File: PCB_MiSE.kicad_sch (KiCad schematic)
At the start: 35 parts, among them IC1 MSP430FR2355TPT, J1 WIFI, J2 Conn_01x03, J4 Clk read conn, J6 Display, J7 I2C read, J8 Conn_02x07_Odd_Even, SW1 SW_Push, SW2 SW_Push, SW3 SW_Push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

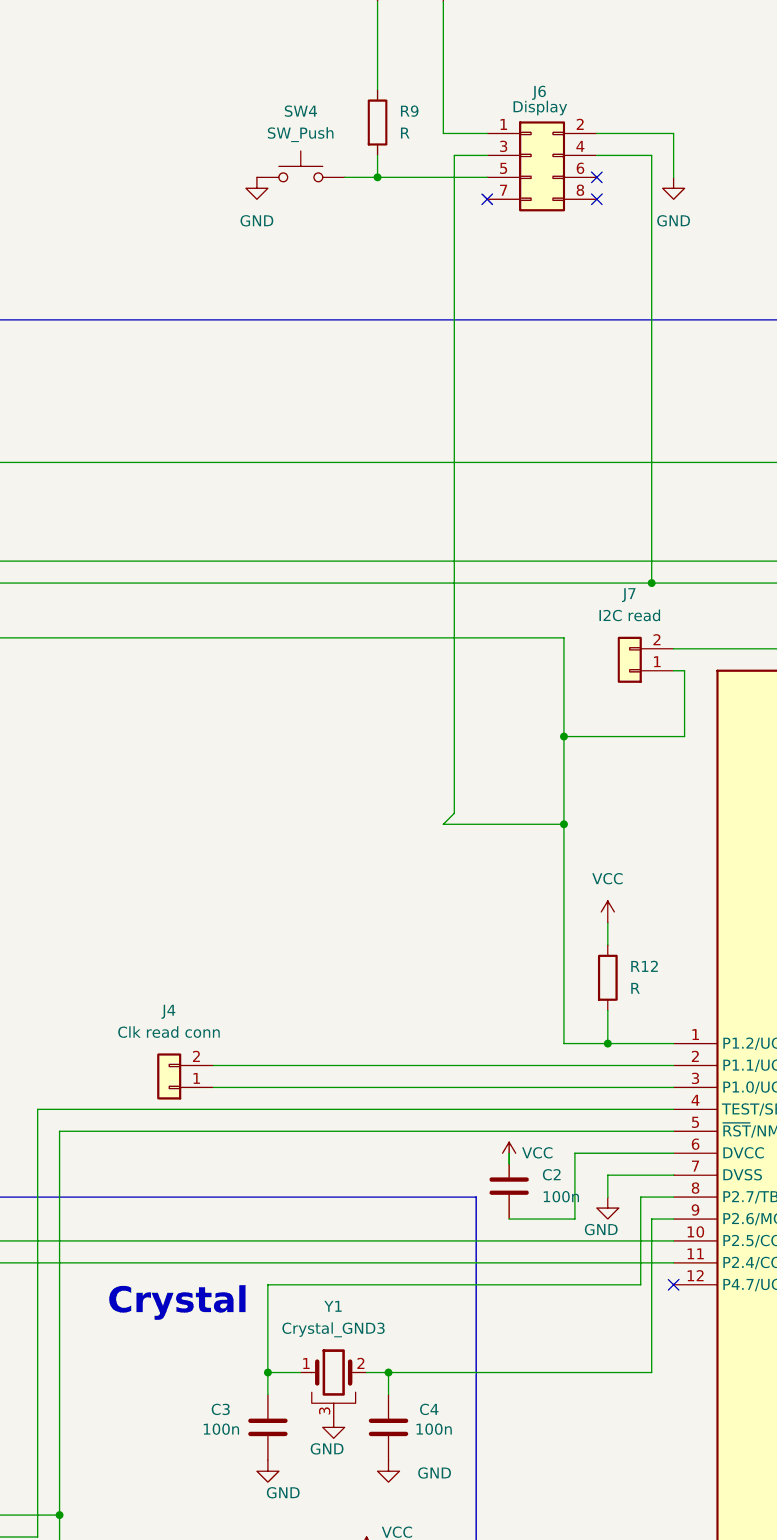
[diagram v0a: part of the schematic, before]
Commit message: Armo layout de PCB y corrijo errores (no errores DRC)
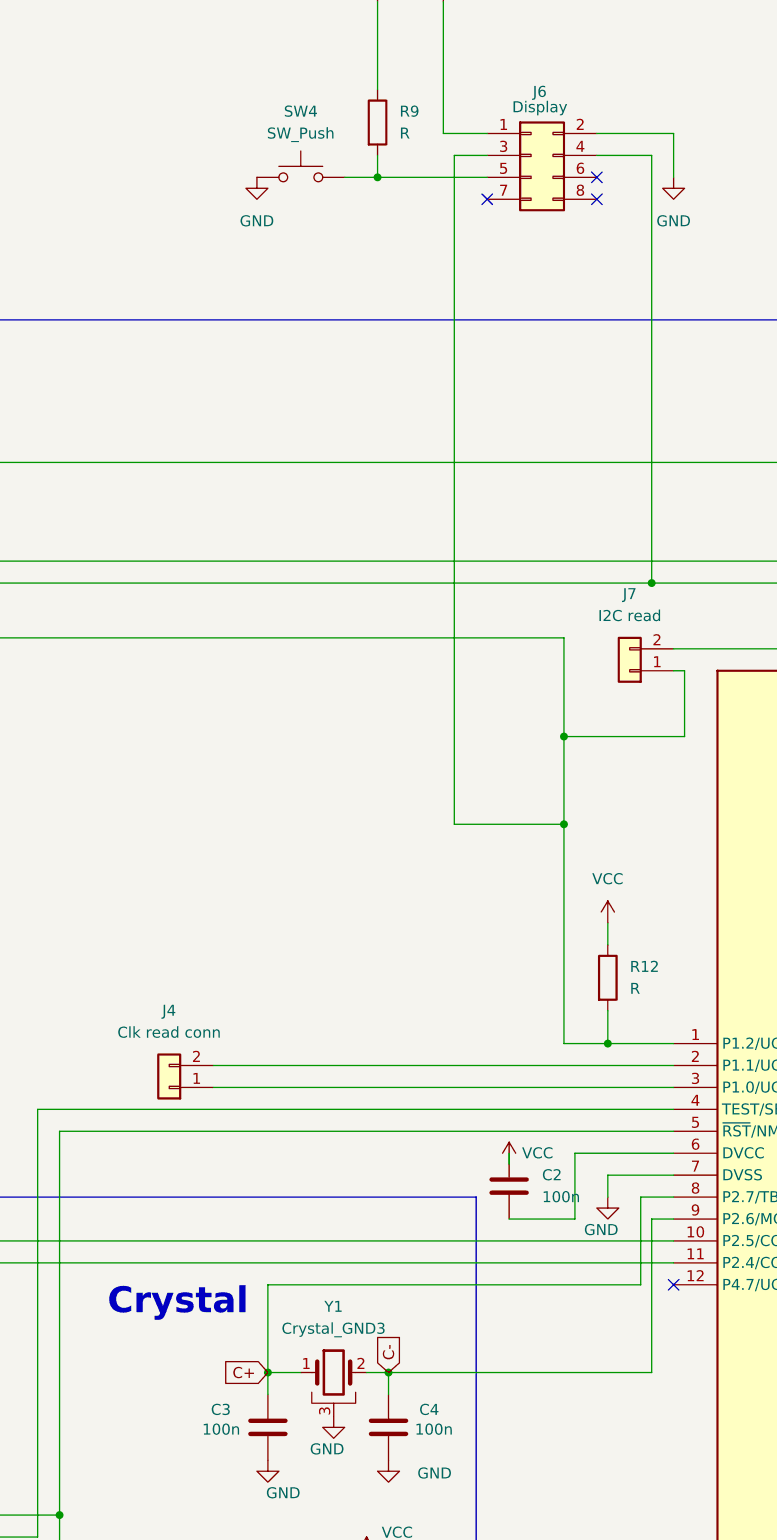
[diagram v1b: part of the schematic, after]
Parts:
- J1: footprint (none) -> Connector_PinSocket_2.54mm:PinSocket_2x04_P2.54mm_Horizontal
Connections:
- net C-: now reaches C4.1, IC1.9 (P2.6/MCLK/XOUT), Y1.2
- net C+: now reaches C3.1, IC1.8 (P2.7/TB0CLK/XIN), Y1.1
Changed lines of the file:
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@@
 	(wire
 		(pts
+			(xy 220.98 167.64) (xy 233.68 167.64)
+		)
+		(stroke
+			(width 0)
+			(type default)
+		)
+	)
+	(wire
+		(pts
 			(xy 101.6 276.86) (xy 101.6 275.59)
 		)
@@
 	(wire
 		(pts
-			(xy 220.98 90.17) (xy 220.98 166.37)
+			(xy 220.98 90.17) (xy 220.98 167.64)
 		)
 		(stroke
@@
 	(wire
 		(pts
-			(xy 219.71 167.64) (xy 233.68 167.64)
-		)
-		(stroke
-			(width 0)
-			(type default)
-		)
-	)
-	(wire
-		(pts
 			(xy 238.76 193.04) (xy 246.38 193.04)
 		)
@@
 	(wire
 		(pts
-			(xy 220.98 166.37) (xy 219.71 167.64)
-		)
-		(stroke
-			(width 0)
-			(type default)
-		)
-	)
-	(wire
-		(pts
 			(xy 50.8 125.73) (xy 50.8 128.27)
 		)
@@
 		)
 	)
+	(global_label "C+"
+		(shape input)
+		(at 199.39 231.14 180)
+		(fields_autoplaced yes)
+		(effects
+			(font
+				(size 1.27 1.27)
+			)
+			(justify right)
+		)
+		(property "Intersheetrefs" "${INTERSHEET_REFS}"
+			(at 193.5624 231.14 0)
+			(effects
+				(font
+					(size 1.27 1.27)
+				)
+				(justify right)
+				(hide yes)
+			)
+		)
+	)
+	(global_label "C-"
+		(shape input)
+		(at 213.36 231.14 90)
+		(fields_autoplaced yes)
+		(effects
+			(font
+				(size 1.27 1.27)
+			)
+			(justify left)
+		)
+		(property "Intersheetrefs" "${INTERSHEET_REFS}"
+			(at 213.36 225.3124 90)
+			(effects
+				(font
+					(size 1.27 1.27)
+				)
+				(justify left)
+				(hide yes)
+			)
+		)
+	)
 	(global_label "GPIOl'"
 		(shape input)
@@
 			)
 		)
-		(property "Footprint" ""
+		(property "Footprint" "Connector_PinSocket_2.54mm:PinSocket_2x04_P2.54mm_Horizontal"
 			(at 548.64 222.25 0)
 			(effects

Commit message: Modifico footprint del wifi
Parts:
- J1: footprint Connector_PinSocket_2.54mm:PinSocket_2x04_P2.54mm_Horizontal -> Connector_PinHeader_2.54mm:PinHeader_2x04_P2.54mm_Vertical
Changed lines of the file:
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@@
 			)
 		)
-		(property "Footprint" "Connector_PinSocket_2.54mm:PinSocket_2x04_P2.54mm_Horizontal"
+		(property "Footprint" "Connector_PinHeader_2.54mm:PinHeader_2x04_P2.54mm_Vertical"
 			(at 548.64 222.25 0)
 			(effects
